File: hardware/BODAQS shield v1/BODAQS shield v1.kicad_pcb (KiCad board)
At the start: 2 copper layers, 60 x 99 mm, 60 parts, among them J1 Analog Input 1, J10 Reset, J2 Reset, J3 Bar switch, J4 Navigation pad, J5 I2C Breakout, J6 Analog Input 2, J7 Analog Input 3, J8 Analog Input 4, J9 UART Breakout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

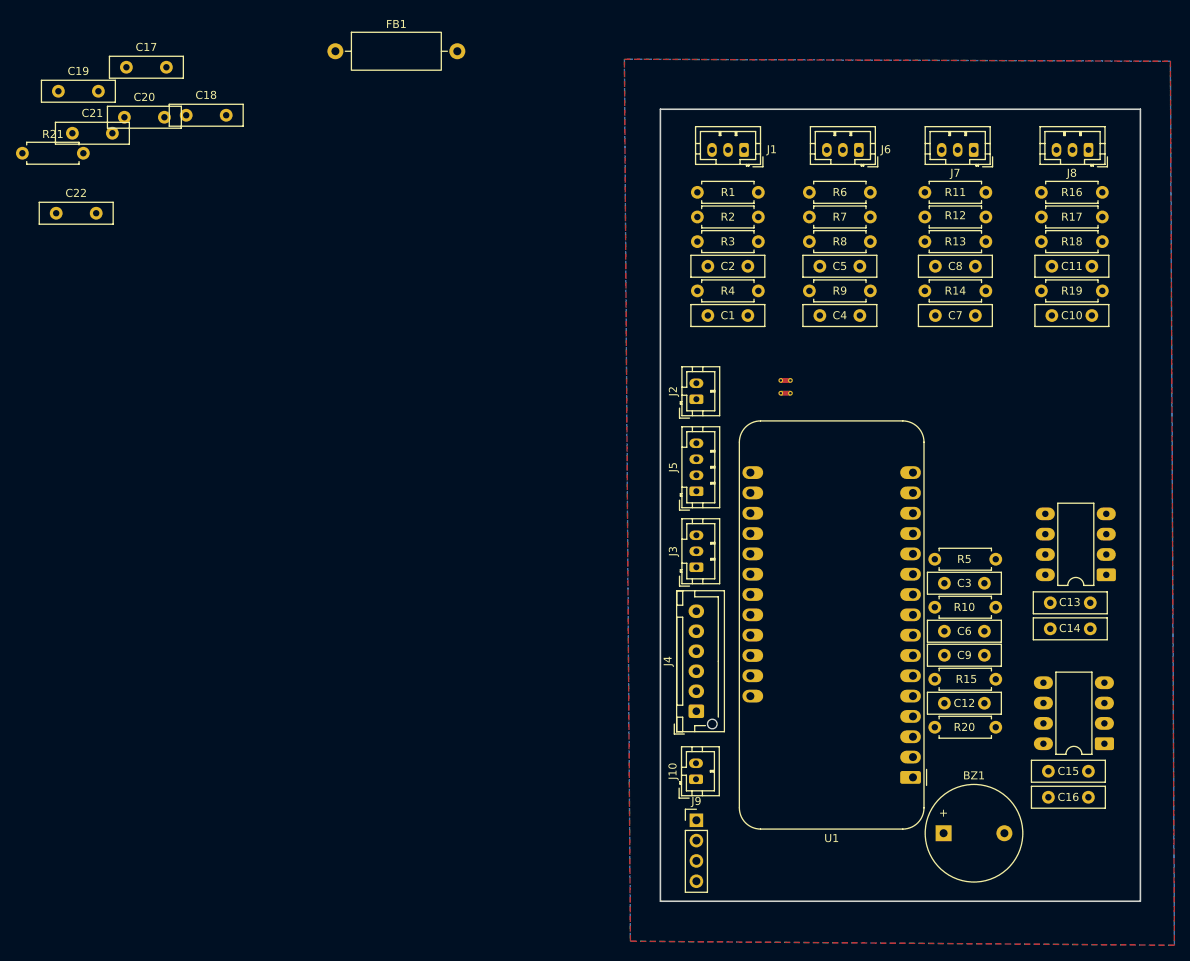
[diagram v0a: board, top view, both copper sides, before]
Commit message: Support SDMMA and SDFat
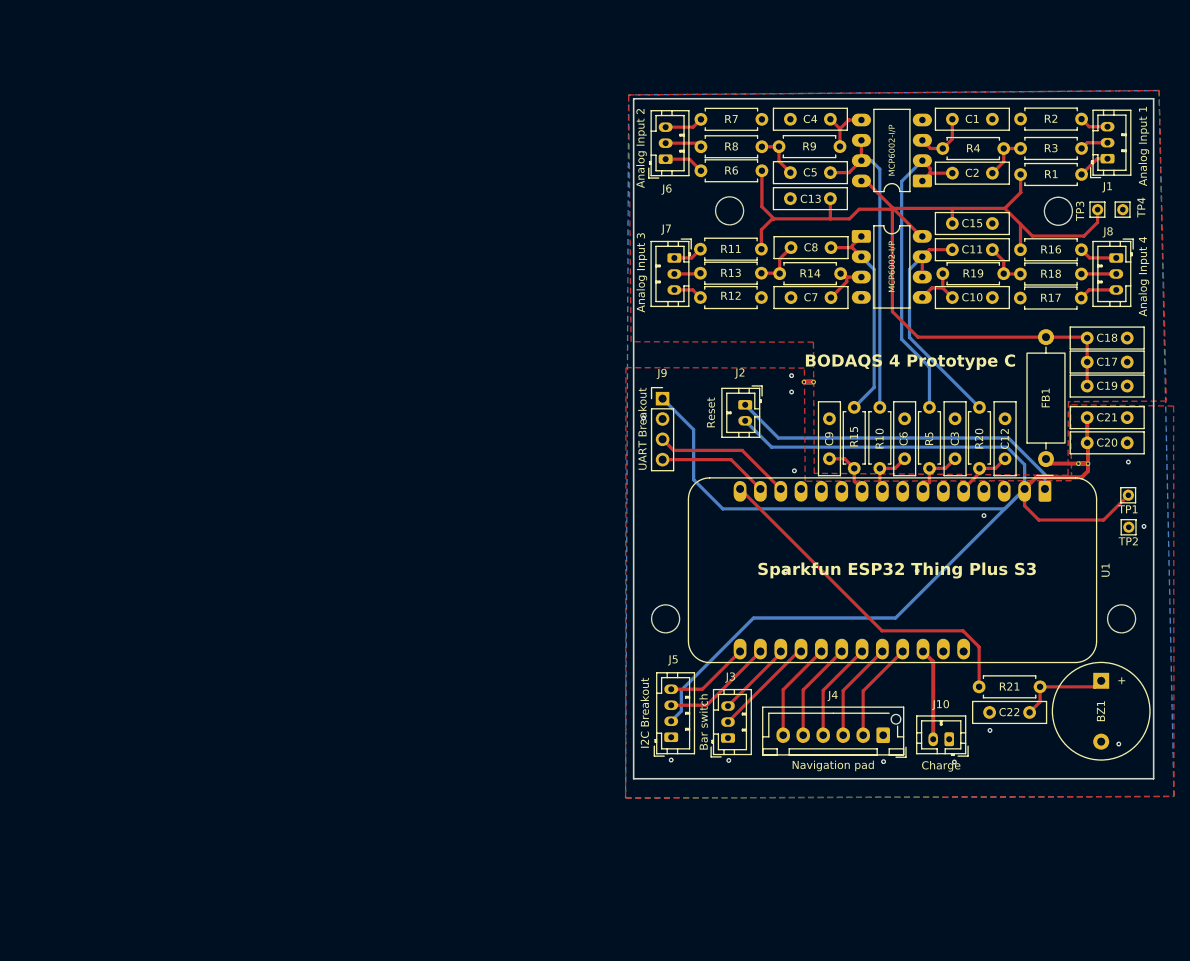
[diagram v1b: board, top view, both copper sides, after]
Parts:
- removed C14, C16: 10uF, Capacitor_THT:C_Disc_D9.0mm_W2.5mm_P5.00mm
- added ?: , , F.Cu at (190.5, 55.8)
- added ?: , , F.Cu at (149.4, 55.7)
- added ?: , , F.Cu at (141.4, 106.7)
- added ?: , , F.Cu at (198.4, 106.7)
- added TP1: TestPoint, Connector_Pin:Pin_D0.7mm_L6.5mm_W1.8mm_FlatFork, F.Cu at (199.2, 91.2)
- added TP2: TestPoint, Connector_Pin:Pin_D0.7mm_L6.5mm_W1.8mm_FlatFork, F.Cu at (199.3, 95.2)
- added TP3: TestPoint, Connector_Pin:Pin_D0.7mm_L6.5mm_W1.8mm_FlatFork, F.Cu at (195.4, 55.5)
- added TP4: TestPoint, Connector_Pin:Pin_D0.7mm_L6.5mm_W1.8mm_FlatFork, F.Cu at (198.6, 55.5)
- J10: value Reset -> Charge
- moved R21 136.9 mm to (180.6, 115.2)
- moved C22 136.7 mm to (186.9, 118.4), turned to 180 degrees
- moved C19 133.8 mm to (194.1, 77.6)
- moved C21 131.7 mm to (194.1, 81.5)
- moved C20 127.0 mm to (194.1, 84.7)
- moved C17 125.6 mm to (194.1, 74.6)
- moved C18 116.0 mm to (194.1, 71.6)
- moved FB1 102.4 mm to (188.9, 86.7), turned to 90 degrees
- moved U3 70.3 mm to (165.9, 58.9), turned to 0 degrees
- moved C15 69.5 mm to (177.2, 57.3)
- moved C13 57.5 mm to (162.0, 54.2), turned to 180 degrees
- moved U2 54.3 mm to (173.5, 52.0)
- moved J9 52.9 mm to (141.0, 79.2)
- moved R2 49.6 mm to (193.4, 44.2), turned to 180 degrees
- moved J1 45.4 mm to (196.6, 49.2), turned to 90 degrees
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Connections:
- U1 pad 10: ANALOG1 -> ANALOG3
- U1 pad 12: BUZZER -> unconnected-(U1-GPIO11-Pad12)
- U1 pad 16: unconnected-(U1-GPIO42-Pad16) -> BUZZER
- U1 pad 27: +3V3 -> unconnected-(U1-3V3EN-Pad27)
- U1 pad 7: ANALOG3 -> ANALOG1
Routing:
- net +3V3: track 0.00 -> 186.3 mm
- net A3V3: track 0.00 -> 123.8 mm
- net BUZZER: track 0.00 -> 43.0 mm
- net RESET: track 0.00 -> 42.9 mm
- net Net-(U2B--): track 0.00 -> 39.6 mm
- net Net-(U2A--): track 0.00 -> 39.5 mm
- net Net-(U3B--): track 0.00 -> 29.8 mm
- net Net-(U3A--): track 0.00 -> 26.7 mm
- net RXI: track 0.00 -> 17.3 mm
- net SCL: track 0.00 -> 13.9 mm
- net  TXO: track 0.00 -> 13.8 mm
- net Mark: track 0.00 -> 12.8 mm
- net Enter: track 0.00 -> 12.5 mm
- net Right: track 0.00 -> 12.5 mm
- net Left: track 0.00 -> 12.5 mm
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- added copper zone on F.Cu, net AGND
- added copper zone on B.Cu, net GND
- removed copper zone on B.Cu, net AGND
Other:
- board size 60 x 99 mm -> 65 x 85 mm
- board text added: "BODAQS 4 Prototype C"
- board text added: "Sparkfun ESP32 Thing Plus S3"
